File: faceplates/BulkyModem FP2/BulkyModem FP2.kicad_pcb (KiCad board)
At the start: 2 copper layers, 100 x 23.2 mm, 6 parts, among them M1 Mounting_Pin, M2 Mounting_Pin, M3 Mounting_Pin, M4 Mounting_Pin

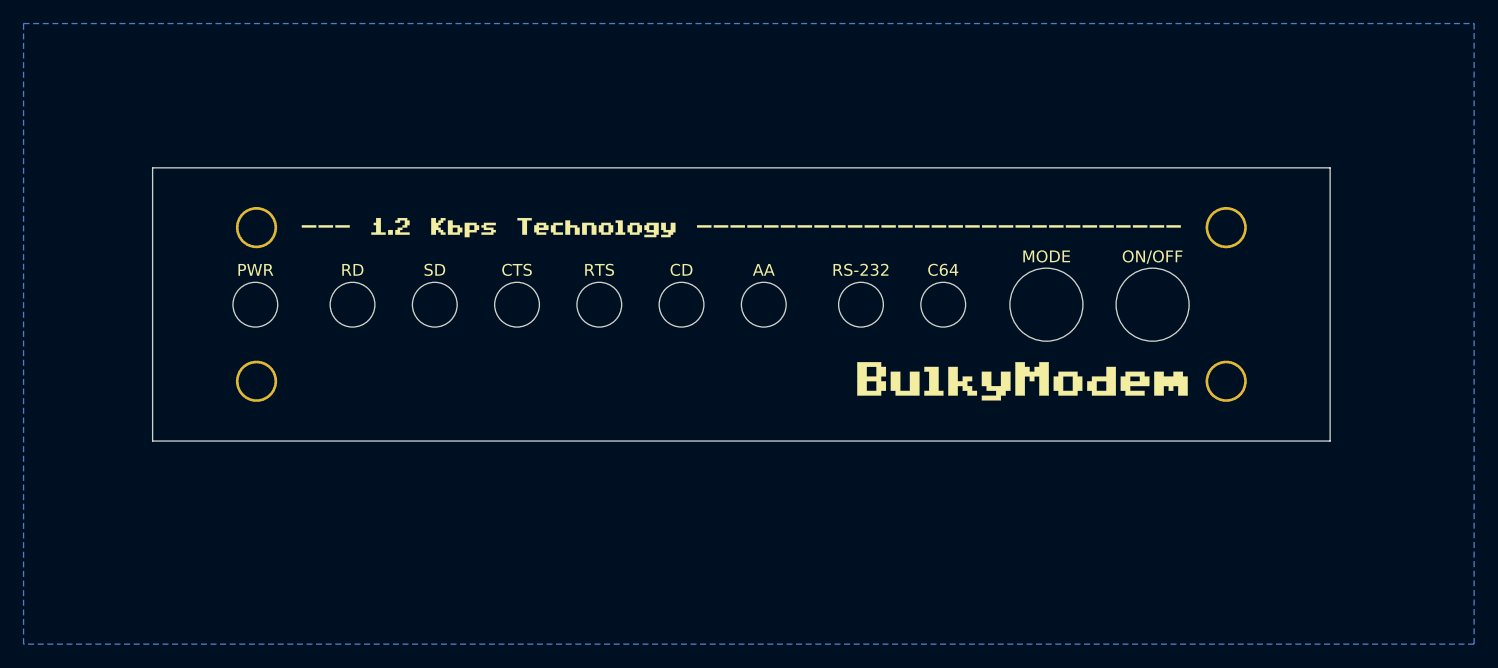
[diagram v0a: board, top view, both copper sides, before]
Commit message: Revised version. Mainly buffering signals
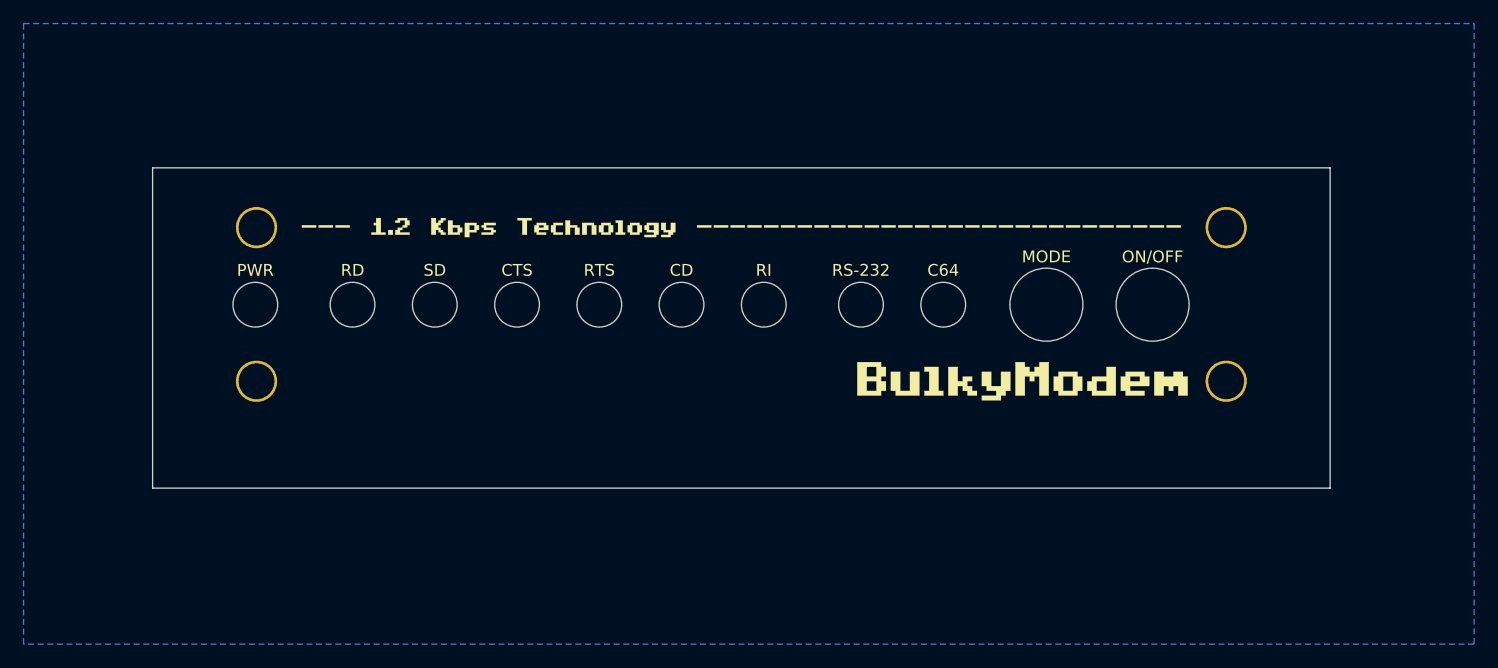
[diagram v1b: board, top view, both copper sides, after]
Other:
- board size 100 x 23.2 mm -> 100 x 27.2 mm
- board text added: "BulkyModem Front Panel FP2 (rev. B) github.com/tebl"
- board text added: "JLCJLCJLCJLC"
- board text added: "RI"
- board text added: "WayWayWay"
- board text removed: "AA"
- board text removed: "BulkyModem Front Panel FP2 (rev. A) github.com/tebl"
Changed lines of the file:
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@@
   (general
     (thickness 1.6)
-    (drawings 27)
+    (drawings 30)
     (tracks 0)
     (zones 0)
@@
       (net 1 GND) (solder_mask_margin 0.8))
   )
+  (gr_text WayWayWay (at 169.74 133.159) (layer B.SilkS)
+    (effects (font (size 0.9 0.9) (thickness 0.1)) (justify mirror))
+  )
+  (gr_text JLCJLCJLCJLC (at 112.59 133.159) (layer F.Fab)
+    (effects (font (size 0.9 0.9) (thickness 0.1)) (justify mirror))
+  )
+  (gr_line (start 91.09 138.174) (end 191.09 138.174) (layer Edge.Cuts) (width 0.05))
   (gr_circle (center 166.998 122.595) (end 170.098 122.595) (layer Edge.Cuts) (width 0.05))
   (gr_text MODE (at 166.998 118.531) (layer F.SilkS)
@@
   )
   (gr_circle (center 142.995 122.595) (end 144.895 122.595) (layer Edge.Cuts) (width 0.05))
-  (gr_text AA (at 142.995 119.674) (layer F.SilkS)
+  (gr_text RI (at 142.995 119.674) (layer F.SilkS)
     (effects (font (size 1 1) (thickness 0.15)))
   )
@@
     (effects (font (size 1 1) (thickness 0.15)))
   )
-  (gr_text "BulkyModem\nFront Panel FP2 (rev. A)\ngithub.com/tebl" (at 94.1 122.849 270) (layer B.SilkS)
+  (gr_text "BulkyModem\nFront Panel FP2 (rev. B)\ngithub.com/tebl" (at 94.1 122.849 270) (layer B.SilkS)
     (effects (font (size 0.8 0.8) (thickness 0.1)) (justify mirror))
   )
   (gr_line (start 91.09 110.974) (end 191.09 110.974) (layer Edge.Cuts) (width 0.05))
-  (gr_line (start 91.09 134.174) (end 191.09 134.174) (layer Edge.Cuts) (width 0.05))
-  (gr_line (start 91.09 110.974) (end 91.09 134.174) (layer Edge.Cuts) (width 0.05))
-  (gr_line (start 191.09 134.174) (end 191.09 110.974) (layer Edge.Cuts) (width 0.05))
+  (gr_line (start 91.09 134.174) (end 191.09 134.174) (layer Dwgs.User) (width 0.05))
+  (gr_line (start 91.09 110.974) (end 91.09 138.174) (layer Edge.Cuts) (width 0.05))
+  (gr_line (start 191.09 138.174) (end 191.09 110.974) (layer Edge.Cuts) (width 0.05))
   (zone (net 1) (net_name GND) (layer B.Cu) (hatch edge 0.508)
     (connect_pads (clearance 0.508))

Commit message: TTL legend
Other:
- net class Default removed
- net class PWR removed
